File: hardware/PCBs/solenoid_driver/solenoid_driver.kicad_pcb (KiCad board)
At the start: 2 copper layers, 45.5 x 48.5 mm, 23 parts, among them J1 from_mainboard, J2 12V power, J3 to_solenoid2, J4 to_solenoid1, J5 12V power, Q1 Q_NMOS_GDS, Q2 Q_NMOS_GDS

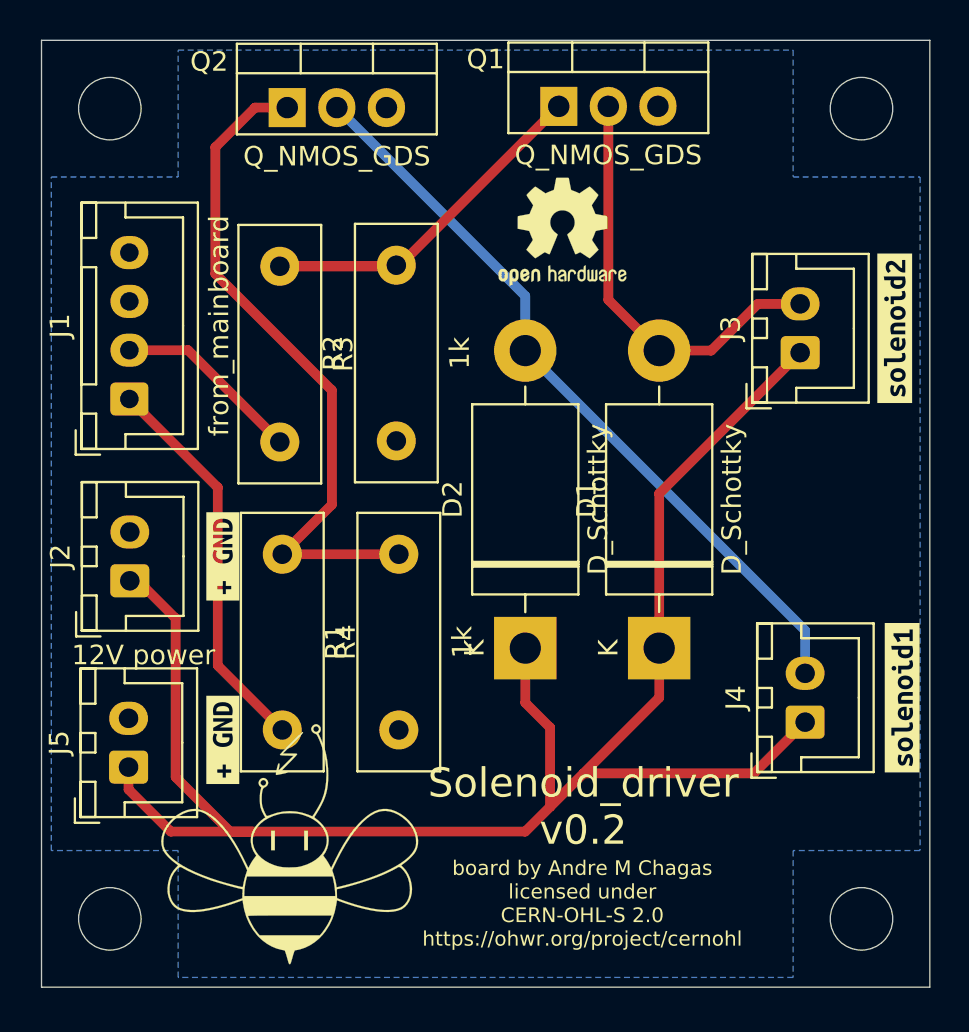
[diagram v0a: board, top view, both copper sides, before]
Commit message: Update solenoid driver to v0.3
Update solenoid driver to v0.3:
- added driver IC and peripherals
- rearrangements in the board layout

Co-Authored-By: Andre Maia Chagas <a.maia-chagas@sussex.ac.uk>
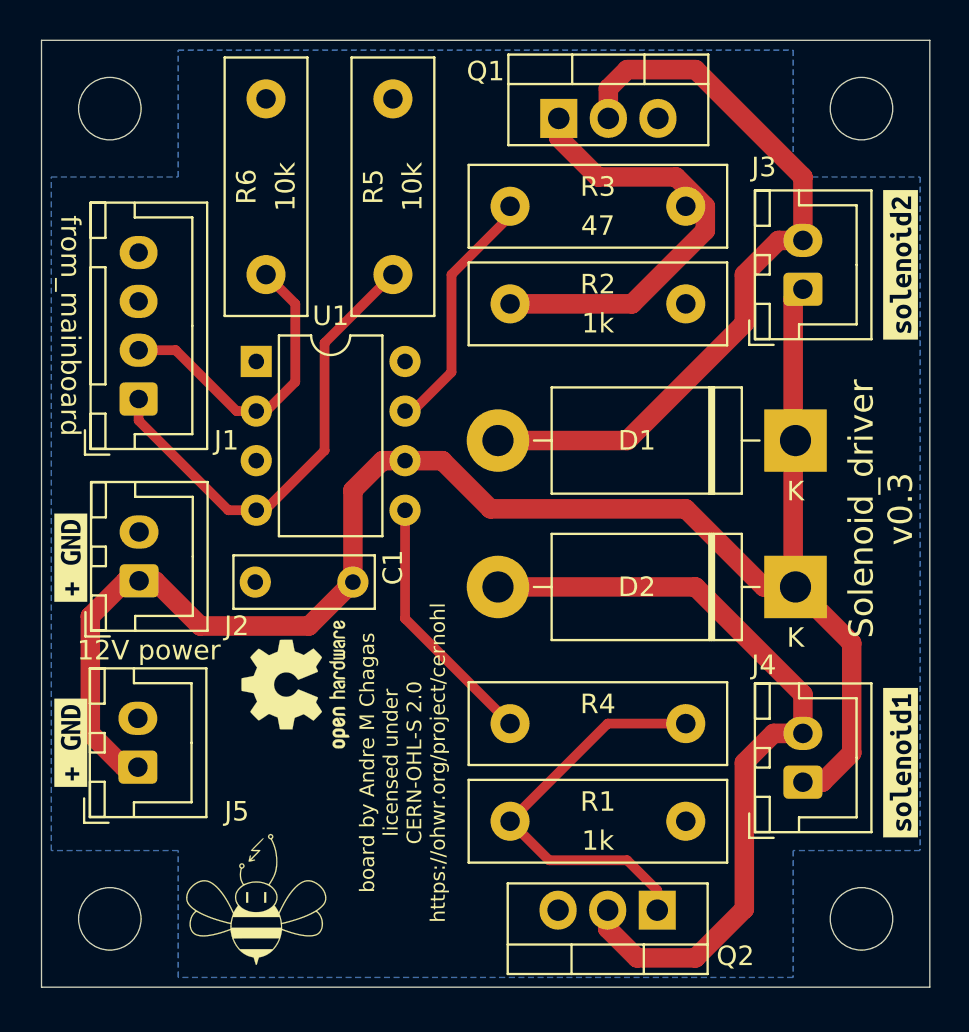
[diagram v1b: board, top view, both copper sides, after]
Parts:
- removed the G*** at (124.7, 121.7)
- added C1: 100nF, Capacitor_THT:C_Disc_D7.0mm_W2.5mm_P5.00mm, F.Cu at (128.0, 108.2)
- added G***: LOGO, logo-beehive:logo-beehive-7_2х6_7mm, F.Cu at (123.0, 124.5)
- added R5: 10k, Resistor_THT:R_Box_L13.0mm_W4.0mm_P9.00mm, F.Cu at (130.0, 83.5)
- added R6: 10k, Resistor_THT:R_Box_L13.0mm_W4.0mm_P9.00mm, F.Cu at (123.5, 83.5)
- added U1: MIC4427, Package_DIP:DIP-8_W7.62mm, F.Cu at (123.0, 97.0)
- moved Q2 45.3 mm to (143.5, 125.1), turned to 180 degrees
- moved REF** 26.9 mm to (125.0, 113.5), turned to 90 degrees
- moved R4 22.4 mm to (145.0, 115.5), turned to 180 degrees
- moved R3 21.0 mm to (145.0, 89.0), turned to 180 degrees
- moved R2 16.4 mm to (145.0, 94.0), turned to 180 degrees
- moved R1 15.4 mm to (145.0, 120.5), turned to 180 degrees
- moved D2 14.2 mm to (150.6, 108.5), turned to 180 degrees
- moved D1 12.7 mm to (150.6, 101.0), turned to 180 degrees
- moved kibuzzard-63064EFA 7.79 mm to (113.5, 116.5)
- moved kibuzzard-63065932 7.79 mm to (113.5, 107.0)
- moved kibuzzard-63063C94 3.33 mm to (156.0, 117.5)
- moved kibuzzard-63064E8E 3.26 mm to (156.0, 92.0)
- moved J3 3.25 mm to (151.0, 93.2)
- moved J4 3.08 mm to (151.0, 118.5)
- moved Q1 0.62 mm to (138.5, 84.5)
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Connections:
- J1 pad 1: solenoid1 -> Net-(J1-Pad1)
- J1 pad 2: solenoid2 -> Net-(U1-Pad2)
- R3 pad 2: solenoid2 -> solenoid1
- R4 pad 2: solenoid1 -> solenoid2
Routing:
- net Net-(J1-Pad1): track 0.00 -> 24.3 mm
- net Net-(D1-Pad2): track 21.8 -> 38.8 mm
- net Net-(U1-Pad2): track 0.00 -> 16.1 mm
- net Net-(Q2-Pad1): track 35.1 -> 21.1 mm
- net solenoid1: track 20.2 -> 13.2 mm
- net +12V: track 90.2 -> 84.2 mm
- net solenoid2: track 9.65 -> 13.2 mm
- net Net-(Q1-Pad1): track 24.2 -> 22.3 mm
- net Net-(D2-Pad2): track 38.9 -> 40.7 mm
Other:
- board text added: "Solenoid_driver v0.3"
- board text removed: "Solenoid_driver v0.2"
